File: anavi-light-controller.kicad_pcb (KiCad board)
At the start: 2 copper layers, 74.9 x 40.6 mm, 27 parts, among them J1 Screw_Terminal_1x04, P1 CONN_01X03, Q1 IRF8721PBF-1, Q2 IRF8721PBF-1, Q3 IRF8721PBF-1, SW1 SW_DIP_x01, U1 I2C_SENS_1, U2 I2C_SENS_1, U3 I2C_SENS_1

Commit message: rev1.2: Use SMD footprint for ESP-12E
Use SMD footprint for ESP-12E to simplify the
assembly, updated product version and routing.

Signed-off-by: Leon Anavi <leon@anavi.org>
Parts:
- ESP-12: footprint ESP8266:ESP-12E -> ESP8266:ESP-12E_SMD
- moved R4 0.81 mm to (108.5, 79.5), turned to 270 degrees
- moved R5 0.57 mm to (108.5, 84.1)
- moved R6 0.57 mm to (108.5, 89.2)
- moved ESP-12 0.51 mm to (97.2, 81.0)
- moved J1 0.25 mm to (136.7, 98.9)
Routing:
- net +3V3: track 97.8 -> 88.7 mm, vias 0 -> 2
- net Net-(Q3-Pad4): track 24.9 -> 19.2 mm
- net GND: track 3.24 -> 0.00 mm
- net Net-(ESP-12-Pad14): track 42.1 -> 40.5 mm
- net Net-(ESP-12-Pad13): track 40.6 -> 39.3 mm
- net Net-(ESP-12-Pad5): track 22.6 -> 21.7 mm
- net Net-(ESP-12-Pad7): track 27.6 -> 28.5 mm
- net Net-(Q1-Pad4): track 21.9 -> 21.2 mm
- net Net-(Q2-Pad4): track 17.6 -> 16.9 mm
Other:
- board text added: "Rev. 1.2 (c) 2018"
- board text removed: "Rev. 1.1 (c) 2017"

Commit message: anavi-light-controller.kicad_pcb: Keepout zones
Add keepout zones below the ESP-12 antenna.

Signed-off-by: Leon Anavi <leon@anavi.org>
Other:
- board text added: "100nF"
- board text added: "10uF"
- board text added: "220R"
- board text added: "IRF8721PBF"
- board text added: "KP-3216EC"
- board text added: "LD1117S33TR"
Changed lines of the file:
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@@
     (area 50.8 67.31 152.400001 114.935001)
     (thickness 1.6)
-    (drawings 18)
+    (drawings 28)
     (tracks 138)
     (zones 0)
@@
     (trace_clearance 0.254)
     (zone_clearance 0.508)
-    (zone_45_only no)
+    (zone_45_only yes)
     (trace_min 0.2)
     (segment_width 0.2)
@@
     (add_net +12V)
   )
+  (module SOT-223 (layer F.Cu)
+    (at 75.438 83.566 270)
+    (descr "module CMS SOT223 4 pins")
+    (tags "CMS SOT")
+    (attr smd)
+    (fp_text reference V1 (at 2.667 2.921 360) (layer F.SilkS)
+      (effects (font (size 0.6 0.6) (thickness 0.15)))
+    )
+    (fp_text value LD1117S33TR (at 0 4.5 270) (layer F.Fab) hide
+      (effects (font (size 1 1) (thickness 0.15)))
+    )
+    (fp_line (start 1.91 3.41) (end 1.91 2.15) (layer F.SilkS) (width 0.12))
+    (fp_line (start 1.91 -3.41) (end 1.91 -2.15) (layer F.SilkS) (width 0.12))
+    (fp_line (start 4.4 -3.6) (end -4.4 -3.6) (layer F.CrtYd) (width 0.05))
+    (fp_line (start 4.4 3.6) (end 4.4 -3.6) (layer F.CrtYd) (width 0.05))
+    (fp_line (start -4.4 3.6) (end 4.4 3.6) (layer F.CrtYd) (width 0.05))
+    (fp_line (start -4.4 -3.6) (end -4.4 3.6) (layer F.CrtYd) (width 0.05))
+    (fp_line (start -1.85 -3.35) (end -1.85 3.35) (layer F.Fab) (width 0.15))
+    (fp_line (start -1.85 3.41) (end 1.91 3.41) (layer F.SilkS) (width 0.12))
+    (fp_line (start -1.85 -3.35) (end 1.85 -3.35) (layer F.Fab) (width 0.15))
+    (fp_line (start -4.1 -3.41) (end 1.91 -3.41) (layer F.SilkS) (width 0.12))
+    (fp_line (start -1.85 3.35) (end 1.85 3.35) (layer F.Fab) (width 0.15))
+    (fp_line (start 1.85 -3.35) (end 1.85 3.35) (layer F.Fab) (width 0.15))
+    (pad 4 smd rect (at 3.15 0 270) (size 2 3.8) (layers F.Cu F.Paste F.Mask))
+    (pad 2 smd rect (at -3.15 0 270) (size 2 1.5) (layers F.Cu F.Paste F.Mask)
+      (net 6 +3V3))
+    (pad 3 smd rect (at -3.15 2.3 270) (size 2 1.5) (layers F.Cu F.Paste F.Mask)
+      (net 9 +12V))
+    (pad 1 smd rect (at -3.15 -2.3 270) (size 2 1.5) (layers F.Cu F.Paste F.Mask)
+      (net 2 GND))
+    (model TO_SOT_Packages_SMD.3dshapes/SOT-223.wrl
+      (at (xyz 0 0 0))
+      (scale (xyz 0.4 0.4 0.4))
+      (rotate (xyz 0 0 90))
+    )
+  )
   (module w_conn_misc:dc_socket (layer F.Cu)
     (at 67.691 95.377 270)
@@
       (effects (font (size 0.6 0.6) (thickness 0.1)))
     )
-    (fp_text value 68R (at 0.0635 0.0635 180) (layer F.Fab)
+    (fp_text value 68R (at 0 -1.651 180) (layer F.Fab)
       (effects (font (size 1 1) (thickness 0.15)))
     )
@@
       (effects (font (size 0.6 0.6) (thickness 0.1)))
     )
-    (fp_text value 4,7K (at 0 0 180) (layer F.Fab)
+    (fp_text value 4,7K (at -0.127 2.667 180) (layer F.Fab)
       (effects (font (size 1 1) (thickness 0.15)))
     )
@@
       (effects (font (size 0.6 0.6) (thickness 0.1)))
     )
-    (fp_text value 4,7K (at 0 0 180) (layer F.Fab)
+    (fp_text value 4,7K (at -0.127 2.667 180) (layer F.Fab)
       (effects (font (size 1 1) (thickness 0.15)))
     )
@@
     )
   )
-  (module SOT-223 (layer F.Cu)
-    (at 75.438 83.566 270)
-    (descr "module CMS SOT223 4 pins")
-    (tags "CMS SOT")
-    (attr smd)
-    (fp_text reference V1 (at 2.667 2.921 360) (layer F.SilkS)
-      (effects (font (size 0.6 0.6) (thickness 0.15)))
-    )
-    (fp_text value LD1117S33TR (at 0 4.5 270) (layer F.Fab) hide
-      (effects (font (size 1 1) (thickness 0.15)))
-    )
-    (fp_line (start 1.91 3.41) (end 1.91 2.15) (layer F.SilkS) (width 0.12))
-    (fp_line (start 1.91 -3.41) (end 1.91 -2.15) (layer F.SilkS) (width 0.12))
-    (fp_line (start 4.4 -3.6) (end -4.4 -3.6) (layer F.CrtYd) (width 0.05))
-    (fp_line (start 4.4 3.6) (end 4.4 -3.6) (layer F.CrtYd) (width 0.05))
-    (fp_line (start -4.4 3.6) (end 4.4 3.6) (layer F.CrtYd) (width 0.05))
-    (fp_line (start -4.4 -3.6) (end -4.4 3.6) (layer F.CrtYd) (width 0.05))
-    (fp_line (start -1.85 -3.35) (end -1.85 3.35) (layer F.Fab) (width 0.15))
-    (fp_line (start -1.85 3.41) (end 1.91 3.41) (layer F.SilkS) (width 0.12))
-    (fp_line (start -1.85 -3.35) (end 1.85 -3.35) (layer F.Fab) (width 0.15))
-    (fp_line (start -4.1 -3.41) (end 1.91 -3.41) (layer F.SilkS) (width 0.12))
-    (fp_line (start -1.85 3.35) (end 1.85 3.35) (layer F.Fab) (width 0.15))
-    (fp_line (start 1.85 -3.35) (end 1.85 3.35) (layer F.Fab) (width 0.15))
-    (pad 4 smd rect (at 3.15 0 270) (size 2 3.8) (layers F.Cu F.Paste F.Mask))
-    (pad 2 smd rect (at -3.15 0 270) (size 2 1.5) (layers F.Cu F.Paste F.Mask)
-      (net 6 +3V3))
-    (pad 3 smd rect (at -3.15 2.3 270) (size 2 1.5) (layers F.Cu F.Paste F.Mask)
-      (net 9 +12V))
-    (pad 1 smd rect (at -3.15 -2.3 270) (size 2 1.5) (layers F.Cu F.Paste F.Mask)
-      (net 2 GND))
-    (model TO_SOT_Packages_SMD.3dshapes/SOT-223.wrl
-      (at (xyz 0 0 0))
-      (scale (xyz 0.4 0.4 0.4))
-      (rotate (xyz 0 0 90))
-    )
-  )
   (module Capacitors_SMD:C_0805_HandSoldering (layer F.Cu)
     (at 76.708 77.724 180)
@@
       (effects (font (size 0.6 0.6) (thickness 0.15)))
     )
-    (fp_text value 2K (at 0 0 90) (layer F.Fab)
+    (fp_text value 2K (at 0.127 1.397 90) (layer F.Fab)
       (effects (font (size 1 1) (thickness 0.15)))
     )
@@
       (rotate (xyz 0 0 0))
     )
+  )
+  (gr_text 10uF (at 76.835 75.057) (layer F.Fab)
+    (effects (font (size 0.8 0.8) (thickness 0.15)))
+  )
+  (gr_text 100nF (at 69.723 84.836) (layer F.Fab)
+    (effects (font (size 0.8 0.8) (thickness 0.15)))
+  )
+  (gr_text 220R (at 108.458 89.154 90) (layer F.Fab)
+    (effects (font (size 0.6 0.8) (thickness 0.15)))
+  )
+  (gr_text 220R (at 108.585 84.201 90) (layer F.Fab)
+    (effects (font (size 0.8 0.8) (thickness 0.2)))
+  )
+  (gr_text 220R (at 108.458 79.629 90) (layer F.Fab)
+    (effects (font (size 0.8 0.8) (thickness 0.2)))
+  )
+  (gr_text KP-3216EC (at 83.693 78.486) (layer F.Fab)
+    (effects (font (size 0.8 0.8) (thickness 0.15)))
+  )
+  (gr_text IRF8721PBF (at 125.857 102.235) (layer F.Fab)
+    (effects (font (size 0.8 0.6) (thickness 0.15)))
+  )
+  (gr_text IRF8721PBF (at 125.857 92.583) (layer F.Fab)
+    (effects (font (size 0.8 0.6) (thickness 0.15)))
+  )
+  (gr_text IRF8721PBF (at 125.857 83.185) (layer F.Fab)
+    (effects (font (size 0.8 0.6) (thickness 0.15)))
+  )
+  (gr_text LD1117S33TR (at 75.438 83.566) (layer F.Fab)
+    (effects (font (size 0.8 0.6) (thickness 0.15)))
   )
   (gr_text 12V (at 77.724 95.25 90) (layer F.SilkS)
@@
       )
     )
+  )
+  (zone (net 0) (net_name "") (layer F.Cu) (hatch edge 0.508)
+    (connect_pads (clearance 0.508))
+    (min_thickness 0.254)
+    (keepout (tracks allowed) (vias allowed) (copperpour not_allowed))
+    (fill (arc_segments 16) (thermal_gap 0.508) (thermal_bridge_width 0.508))
+    (polygon
+      (pts
+        (xy 99.314 79.502) (xy 99.314 96.52) (xy 106.299 96.52) (xy 106.299 78.359) (xy 99.314 78.359)
+        (xy 99.314 79.629)
+      )
+    )
+  )
+  (zone (net 0) (net_name "") (layer B.Cu) (hatch edge 0.508)
+    (connect_pads (clearance 0.508))
+    (min_thickness 0.254)
+    (keepout (tracks allowed) (vias allowed) (copperpour not_allowed))
+    (fill (arc_segments 16) (thermal_gap 0.508) (thermal_bridge_width 0.508))
+    (polygon
+      (pts
+        (xy 106.299 96.52) (xy 99.314 96.52) (xy 99.314 78.359) (xy 106.299 78.359)
+      )
+    )

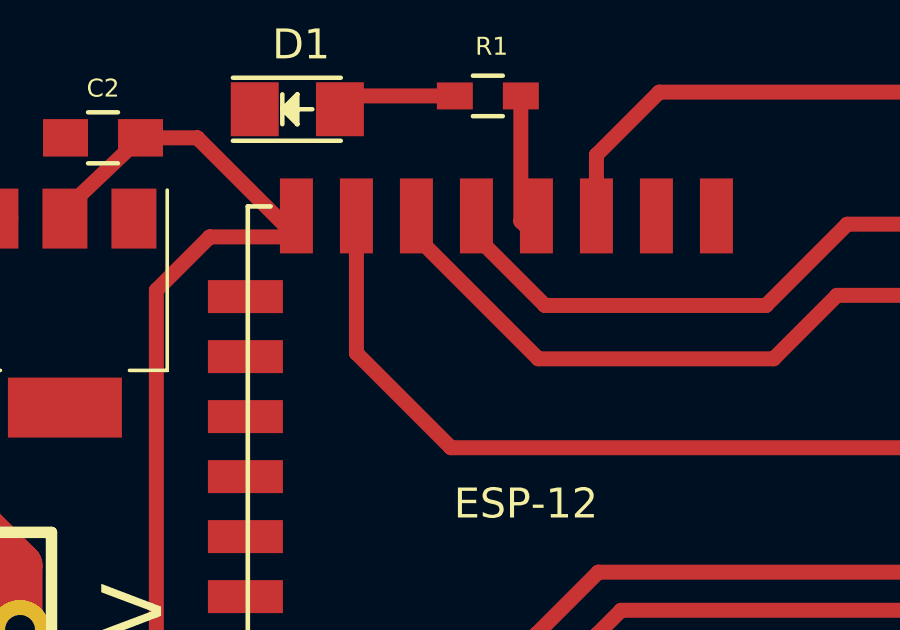
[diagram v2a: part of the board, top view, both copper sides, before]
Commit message: anavi-light-controller.kicad_pcb: Fix ESP12 wiring
Fix the wiring of ESP12 as two pins must be
connected to 3.3V in order to work properly.

Signed-off-by: Leon Anavi <leon@anavi.org>
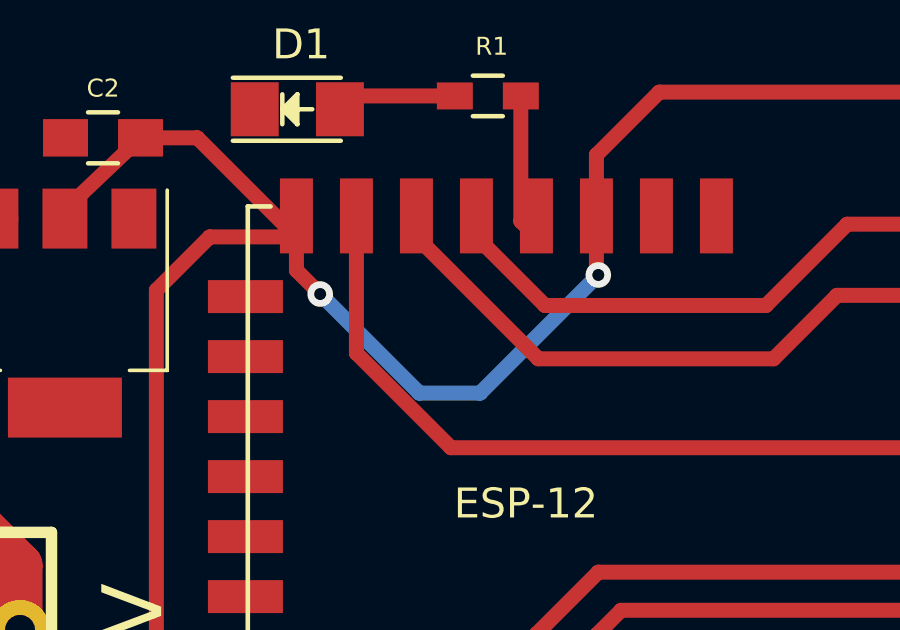
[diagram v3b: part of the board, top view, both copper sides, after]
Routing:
- net +3V3: track 88.7 -> 104.5 mm, vias 2 -> 4
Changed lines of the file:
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@@
   (general
     (links 67)
-    (no_connects 1)
+    (no_connects 0)
     (area 50.8 67.31 152.400001 114.935001)
     (thickness 1.6)
     (drawings 28)
-    (tracks 138)
+    (tracks 147)
     (zones 0)
     (modules 27)
@@
   (segment (start 135.175 94.06) (end 136.652 93.933) (width 1.5) (layer F.Cu) (net 5) (status 20))
   (segment (start 127.635 101.6) (end 135.175 94.06) (width 1.5) (layer F.Cu) (net 5))
+  (segment (start 83.155 81.026) (end 83.155 82.139) (width 0.5) (layer F.Cu) (net 6))
+  (segment (start 93.155 82.233) (end 93.155 81.026) (width 0.5) (layer F.Cu) (net 6))
+  (segment (start 93.218 82.296) (end 93.155 82.233) (width 0.5) (layer F.Cu) (net 6))
+  (via (at 93.218 82.296) (size 0.85) (drill 0.4) (layers F.Cu B.Cu) (net 6))
+  (segment (start 89.281 86.233) (end 93.218 82.296) (width 0.5) (layer B.Cu) (net 6))
+  (segment (start 87.249 86.233) (end 89.281 86.233) (width 0.5) (layer B.Cu) (net 6))
+  (segment (start 83.947 82.931) (end 87.249 86.233) (width 0.5) (layer B.Cu) (net 6))
+  (via (at 83.947 82.931) (size 0.85) (drill 0.4) (layers F.Cu B.Cu) (net 6))
+  (segment (start 83.155 82.139) (end 83.947 82.931) (width 0.5) (layer F.Cu) (net 6))
   (segment (start 83.155 81.026) (end 80.264 81.026) (width 0.5) (layer F.Cu) (net 6))
   (segment (start 78.486 82.804) (end 78.486 103.698) (width 0.5) (layer F.Cu) (net 6))
@@
   (segment (start 78.486 103.698) (end 78.359 103.825) (width 0.5) (layer F.Cu) (net 6))
   (segment (start 93.155 81.026) (end 93.155 78.295) (width 0.5) (layer F.Cu) (net 6))
+  (segment (start 93.155 78.295) (end 95.25 76.2) (width 0.5) (layer F.Cu) (net 6))
+  (segment (start 95.25 76.2) (end 105.664 76.2) (width 0.5) (layer F.Cu) (net 6))
+  (via (at 105.664 76.2) (size 0.85) (drill 0.4) (layers F.Cu B.Cu) (net 6))
+  (segment (start 105.664 76.2) (end 109.474 80.01) (width 0.5) (layer B.Cu) (net 6))
+  (segment (start 109.474 80.01) (end 112.776 80.01) (width 0.5) (layer B.Cu) (net 6))
+  (via (at 112.776 80.01) (size 0.85) (drill 0.4) (layers F.Cu B.Cu) (net 6))
+  (segment (start 112.776 80.01) (end 113.114 79.672) (width 0.5) (layer F.Cu) (net 6))
   (segment (start 113.114 79.672) (end 113.114 78.232) (width 0.5) (layer F.Cu) (net 6))
-  (segment (start 112.776 80.01) (end 113.114 79.672) (width 0.5) (layer F.Cu) (net 6))
-  (via (at 112.776 80.01) (size 0.85) (drill 0.4) (layers F.Cu B.Cu) (net 6))
-  (segment (start 109.474 80.01) (end 112.776 80.01) (width 0.5) (layer B.Cu) (net 6))
-  (segment (start 105.664 76.2) (end 109.474 80.01) (width 0.5) (layer B.Cu) (net 6))
-  (via (at 105.664 76.2) (size 0.85) (drill 0.4) (layers F.Cu B.Cu) (net 6))
-  (segment (start 95.25 76.2) (end 105.664 76.2) (width 0.5) (layer F.Cu) (net 6))
-  (segment (start 93.155 78.295) (end 95.25 76.2) (width 0.5) (layer F.Cu) (net 6))
   (segment (start 77.958 77.724) (end 79.853 77.724) (width 0.5) (layer F.Cu) (net 6))
   (segment (start 79.853 77.724) (end 83.155 81.026) (width 0.5) (layer F.Cu) (net 6))
